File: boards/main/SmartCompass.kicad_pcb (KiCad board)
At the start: 4 copper layers, 70 x 70 mm, 78 parts, among them IC1 Wio-SX1262, J1 SWD HEADER, J3 FH12-10S-0.5SH(55), J4 FH12-10S-0.5SH(55), J5 IPEX, P1 BUTTON_PADS, Q1 DMP2045U, U1 BMD-340-A-R, U2 S25FL064LABNFI043, U3 RT9080-33GJ5, U4 MCP73831T-2ACI_OT, U5 MAX17048G_T10, U6 BNO086, U7 DRV2605LDGSR, U8 MAX-M10S-00B, X1 USB4085-GF-A, Y1 32.768KHZ, Y2 32.768KHZ

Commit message: cleanup
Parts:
- moved ONOFF1 6.96 mm to (81.5, 97.2), turned to -90 degrees
- moved R3 2.31 mm to (119.2, 116.9)
- moved R5 2.12 mm to (117.5, 116.0)
- moved R12 0.67 mm to (81.7, 108.4)
- moved R1 0.67 mm to (117.5, 119.1)
- moved D1 0.50 mm to (82.5, 110.9)
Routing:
- net Net-(ONOFF1-Pin_1): track 30.6 -> 44.6 mm, vias 0 -> 1
- net GND: track 87.2 -> 92.4 mm, vias 92 -> 91
- net Net-(X1-DN1): track 3.69 -> 6.85 mm
- net VBUS: track 145.1 -> 143.1 mm
- net Net-(X1-DP1): track 6.09 -> 4.58 mm
- net /D+: track 30.2 -> 28.7 mm
- net Net-(CHG1-Pad1): track 18.6 -> 19.4 mm
- net Net-(HAPTIC1-Pin_2): track 35.3 -> 34.7 mm
- net +BATT: vias 16 -> 15
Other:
- board text added: "B1"
- board text added: "B2"
- board text added: "B3"
- board text added: "GND"

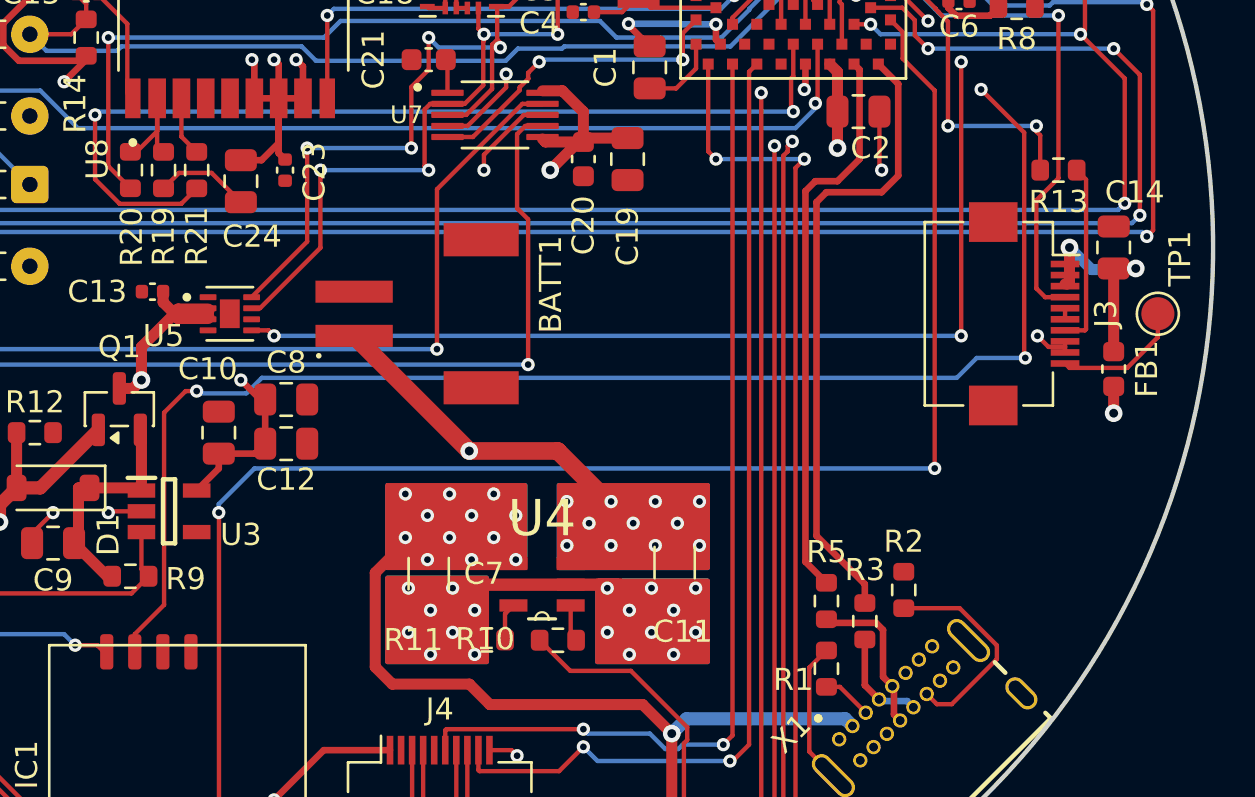
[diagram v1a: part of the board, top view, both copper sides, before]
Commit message: Move the LED ring and haptic engine behind the charge controller, to prevent hot plug ringing from damaging things
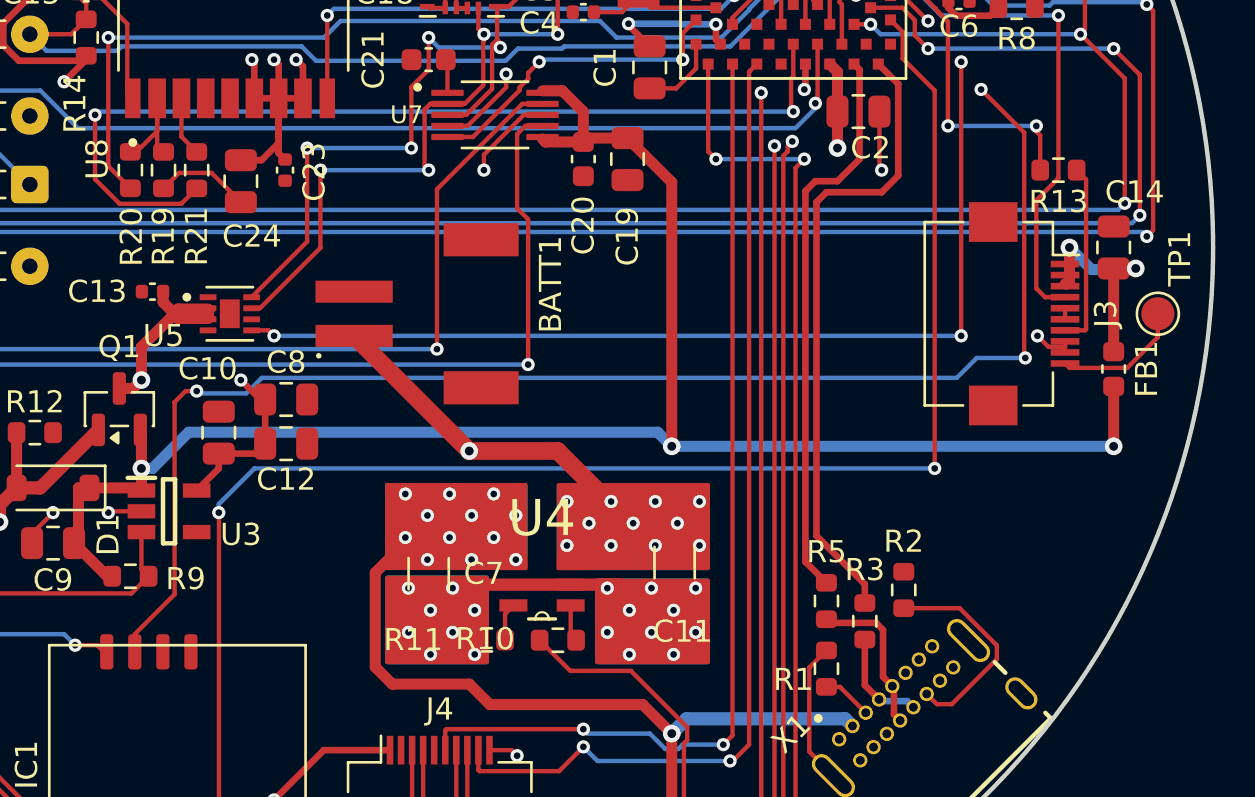
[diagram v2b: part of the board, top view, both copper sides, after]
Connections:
- C19 pad 1: +BATT -> VSYS
- C20 pad 1: +BATT -> VSYS
- C9 pad 1: /Power and USB/VSYS -> VSYS
- D1 pad 1: /Power and USB/VSYS -> VSYS
- FB1 pad 1: +BATT -> VSYS
- Q1 pad 2: /Power and USB/VSYS -> VSYS
- R9 pad 1: /Power and USB/VSYS -> VSYS
- U3 pad 1: /Power and USB/VSYS -> VSYS
- U7 pad 10: +BATT -> VSYS
- U7 pad 6: +BATT -> VSYS
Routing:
- net VSYS: track 0.00 -> 80.0 mm, vias 0 -> 3
- net +BATT: track 94.2 -> 42.1 mm, vias 15 -> 13
- net /Power and USB/VSYS: track 10.2 -> 0.00 mm
